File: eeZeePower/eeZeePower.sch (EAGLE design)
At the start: 11 parts

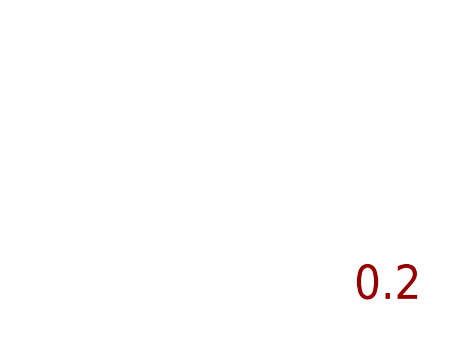
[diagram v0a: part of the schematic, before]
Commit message: Rev 0.3 converted to standard 1206 LED, centered components, mitered corners, moved some components around, removed component names.
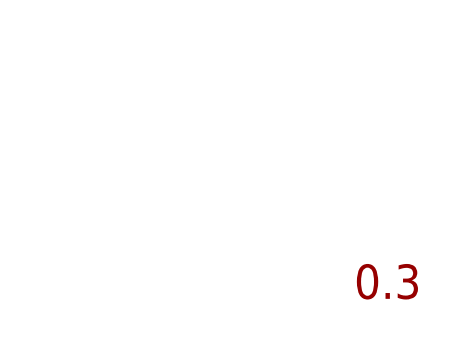
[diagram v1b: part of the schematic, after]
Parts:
- LED1: device led:LEDCHIPLED_0805 -> led:LEDCHIPLED_1206
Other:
- note added: "0.3"
- note removed: "0.2"
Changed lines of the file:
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@@
 <?xml version="1.0" encoding="utf-8"?>
 <!DOCTYPE eagle SYSTEM "eagle.dtd">
-<eagle version="6.3">
+<eagle version="6.4">
 <drawing>
 <settings>
@@
 <grid distance="0.1" unitdist="inch" unit="inch" style="lines" multiple="1" display="no" altdistance="0.01" altunitdist="inch" altunit="inch"/>
 <layers>
-<layer number="1" name="Top" color="4" fill="1" visible="no" active="no"/>
-<layer number="16" name="Bottom" color="1" fill="1" visible="no" active="no"/>
-<layer number="17" name="Pads" color="2" fill="1" visible="no" active="no"/>
-<layer number="18" name="Vias" color="2" fill="1" visible="no" active="no"/>
-<layer number="19" name="Unrouted" color="6" fill="1" visible="no" active="no"/>
-<layer number="20" name="Dimension" color="15" fill="1" visible="no" active="no"/>
-<layer number="21" name="tPlace" color="7" fill="1" visible="no" active="no"/>
-<layer number="22" name="bPlace" color="7" fill="1" visible="no" active="no"/>
-<layer number="23" name="tOrigins" color="15" fill="1" visible="no" active="no"/>
-<layer number="24" name="bOrigins" color="15" fill="1" visible="no" active="no"/>
-<layer number="25" name="tNames" color="7" fill="1" visible="no" active="no"/>
-<layer number="26" name="bNames" color="7" fill="1" visible="no" active="no"/>
-<layer number="27" name="tValues" color="7" fill="1" visible="no" active="no"/>
-<layer number="28" name="bValues" color="7" fill="1" visible="no" active="no"/>
+<layer number="1" name="Top" color="4" fill="1" visible="yes" active="no"/>
+<layer number="16" name="Bottom" color="1" fill="1" visible="yes" active="no"/>
+<layer number="17" name="Pads" color="2" fill="1" visible="yes" active="no"/>
+<layer number="18" name="Vias" color="2" fill="1" visible="yes" active="no"/>
+<layer number="19" name="Unrouted" color="6" fill="1" visible="yes" active="no"/>
+<layer number="20" name="Dimension" color="15" fill="1" visible="yes" active="no"/>
+<layer number="21" name="tPlace" color="7" fill="1" visible="yes" active="no"/>
+<layer number="22" name="bPlace" color="7" fill="1" visible="yes" active="no"/>
+<layer number="23" name="tOrigins" color="15" fill="1" visible="yes" active="no"/>
+<layer number="24" name="bOrigins" color="15" fill="1" visible="yes" active="no"/>
+<layer number="25" name="tNames" color="7" fill="1" visible="yes" active="no"/>
+<layer number="26" name="bNames" color="7" fill="1" visible="yes" active="no"/>
+<layer number="27" name="tValues" color="7" fill="1" visible="yes" active="no"/>
+<layer number="28" name="bValues" color="7" fill="1" visible="yes" active="no"/>
 <layer number="29" name="tStop" color="7" fill="3" visible="no" active="no"/>
 <layer number="30" name="bStop" color="7" fill="6" visible="no" active="no"/>
@@
 <layer number="35" name="tGlue" color="7" fill="4" visible="no" active="no"/>
 <layer number="36" name="bGlue" color="7" fill="5" visible="no" active="no"/>
-<layer number="37" name="tTest" color="7" fill="1" visible="no" active="no"/>
-<layer number="38" name="bTest" color="7" fill="1" visible="no" active="no"/>
+<layer number="37" name="tTest" color="7" fill="1" visible="yes" active="no"/>
+<layer number="38" name="bTest" color="7" fill="1" visible="yes" active="no"/>
 <layer number="39" name="tKeepout" color="4" fill="11" visible="no" active="no"/>
 <layer number="40" name="bKeepout" color="1" fill="11" visible="no" active="no"/>
@@
 <layer number="44" name="Drills" color="7" fill="1" visible="no" active="no"/>
 <layer number="45" name="Holes" color="7" fill="1" visible="no" active="no"/>
-<layer number="46" name="Milling" color="3" fill="1" visible="no" active="no"/>
-<layer number="47" name="Measures" color="7" fill="1" visible="no" active="no"/>
-<layer number="48" name="Document" color="7" fill="1" visible="no" active="no"/>
-<layer number="49" name="Reference" color="7" fill="1" visible="no" active="no"/>
-<layer number="50" name="dxf" color="7" fill="1" visible="no" active="no"/>
-<layer number="51" name="tDocu" color="7" fill="1" visible="no" active="no"/>
-<layer number="52" name="bDocu" color="7" fill="1" visible="no" active="no"/>
-<layer number="53" name="tGND_GNDA" color="7" fill="9" visible="no" active="no"/>
-<layer number="54" name="bGND_GNDA" color="1" fill="9" visible="no" active="no"/>
-<layer number="56" name="wert" color="7" fill="1" visible="no" active="no"/>
+<layer number="46" name="Milling" color="3" fill="1" visible="yes" active="no"/>
+<layer number="47" name="Measures" color="7" fill="1" visible="yes" active="no"/>
+<layer number="48" name="Document" color="7" fill="1" visible="yes" active="no"/>
+<layer number="49" name="Reference" color="7" fill="1" visible="yes" active="no"/>
+<layer number="50" name="dxf" color="7" fill="1" visible="yes" active="no"/>
+<layer number="51" name="tDocu" color="7" fill="1" visible="yes" active="no"/>
+<layer number="52" name="bDocu" color="7" fill="1" visible="yes" active="no"/>
+<layer number="53" name="tGND_GNDA" color="7" fill="9" visible="yes" active="no"/>
+<layer number="54" name="bGND_GNDA" color="1" fill="9" visible="yes" active="no"/>
+<layer number="56" name="wert" color="7" fill="1" visible="yes" active="no"/>
 <layer number="91" name="Nets" color="2" fill="1" visible="yes" active="yes"/>
 <layer number="92" name="Busses" color="1" fill="1" visible="yes" active="yes"/>
@@
 <part name="JP10" library="pinhead-2" deviceset="PINHD-1X03" device="_2.54-S" value="SEL"/>
 <part name="GND2" library="mes" deviceset="GND" device=""/>
-<part name="LED1" library="led" deviceset="LED" device="CHIPLED_0805"/>
+<part name="LED1" library="led" deviceset="LED" device="CHIPLED_1206"/>
 <part name="C1" library="rcl" deviceset="C-US" device="C0603" value="0.1uF"/>
 <part name="C2" library="rcl" deviceset="CPOL-US" device="SMCB" value="100uF"/>
@@
 <plain>
 <text x="160.528" y="23.622" size="3.81" layer="94">eeZee Power</text>
-<text x="233.934" y="24.13" size="3.81" layer="94">0.2</text>
+<text x="233.934" y="24.13" size="3.81" layer="94">0.3</text>
 <text x="55.88" y="134.62" size="1.778" layer="91">NOTE: determine cause of short when rail powered and eeZee Power inserted reverse polarity</text>
 </plain>

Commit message: Converted to standard 1206 10uF, placed input bypass caps on bottom. Rearranged silk, centered pin headers.
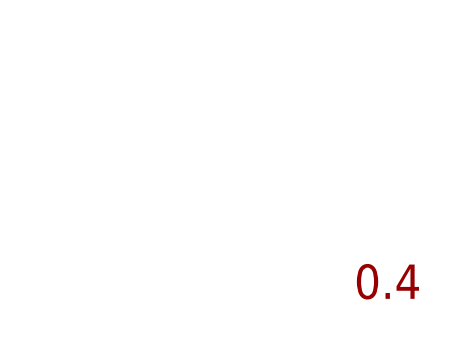
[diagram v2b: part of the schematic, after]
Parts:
- C3: device rcl:C-USC0603 -> rcl:C-USC1206
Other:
- note added: "0.4"
- note removed: "0.3"
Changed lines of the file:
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@@
 <part name="C2" library="rcl" deviceset="CPOL-US" device="SMCB" value="100uF"/>
 <part name="R1" library="resistor" deviceset="R-US_" device="R0603"/>
-<part name="C3" library="rcl" deviceset="C-US" device="C0603" value="10uF"/>
+<part name="C3" library="rcl" deviceset="C-US" device="C1206" value="10uF"/>
 <part name="FRAME1" library="mes" deviceset="LETTER_L" device=""/>
 <part name="C4" library="rcl" deviceset="C-US" device="C0603" value="0.1uF"/>
@@
 <plain>
 <text x="160.528" y="23.622" size="3.81" layer="94">eeZee Power</text>
-<text x="233.934" y="24.13" size="3.81" layer="94">0.3</text>
+<text x="233.934" y="24.13" size="3.81" layer="94">0.4</text>
 <text x="55.88" y="134.62" size="1.778" layer="91">NOTE: determine cause of short when rail powered and eeZee Power inserted reverse polarity</text>
 </plain>

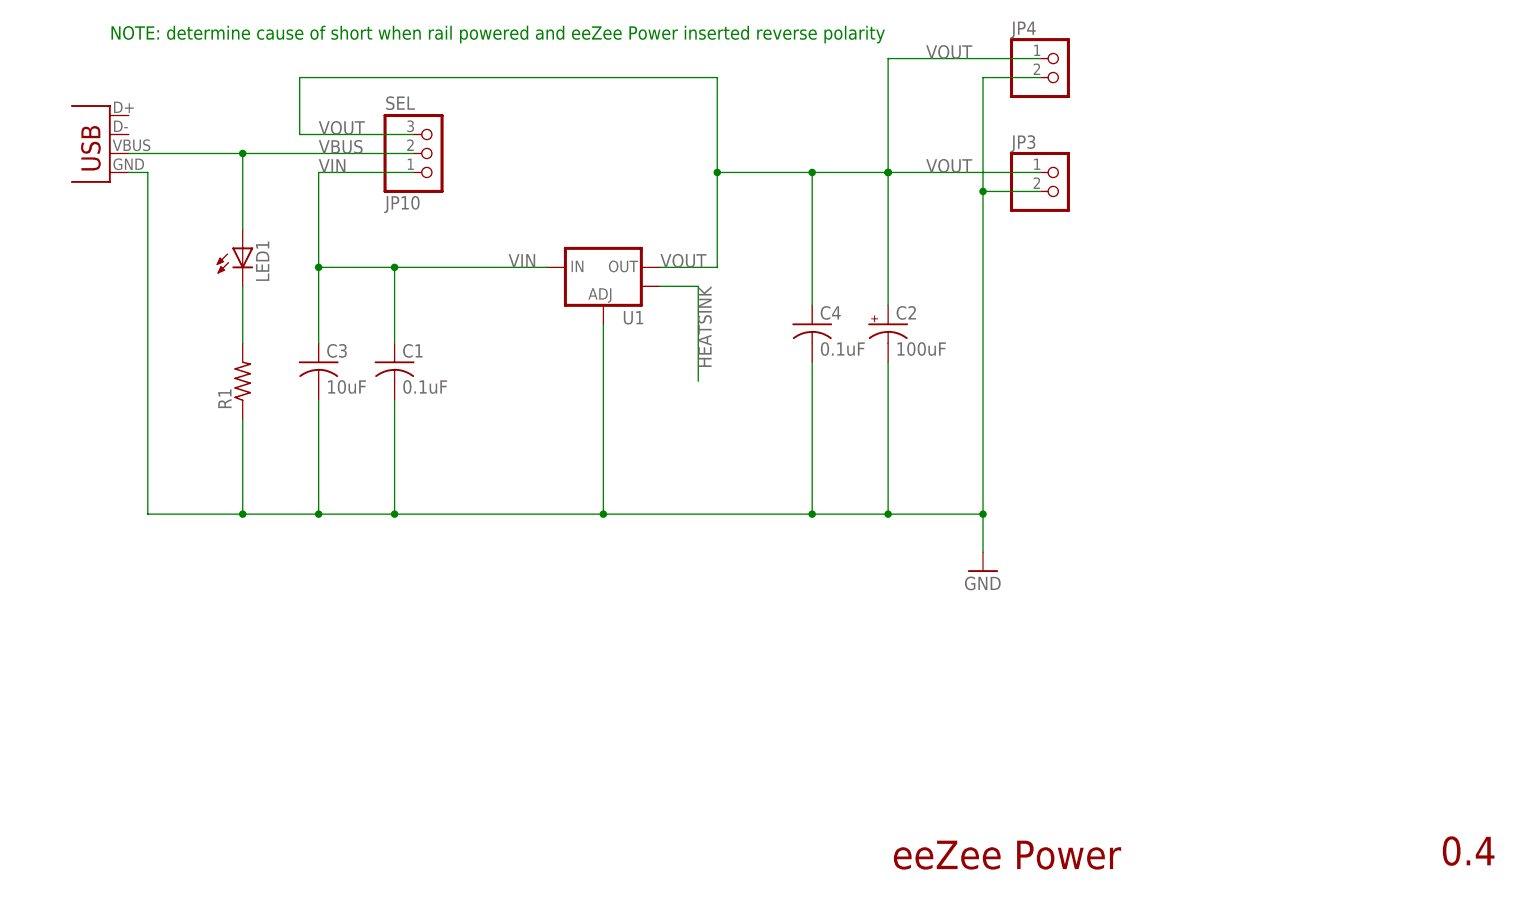
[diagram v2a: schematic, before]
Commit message: Changed to 10mil/8mil spacing, improved thermal design, connected heatsink to VOUT.
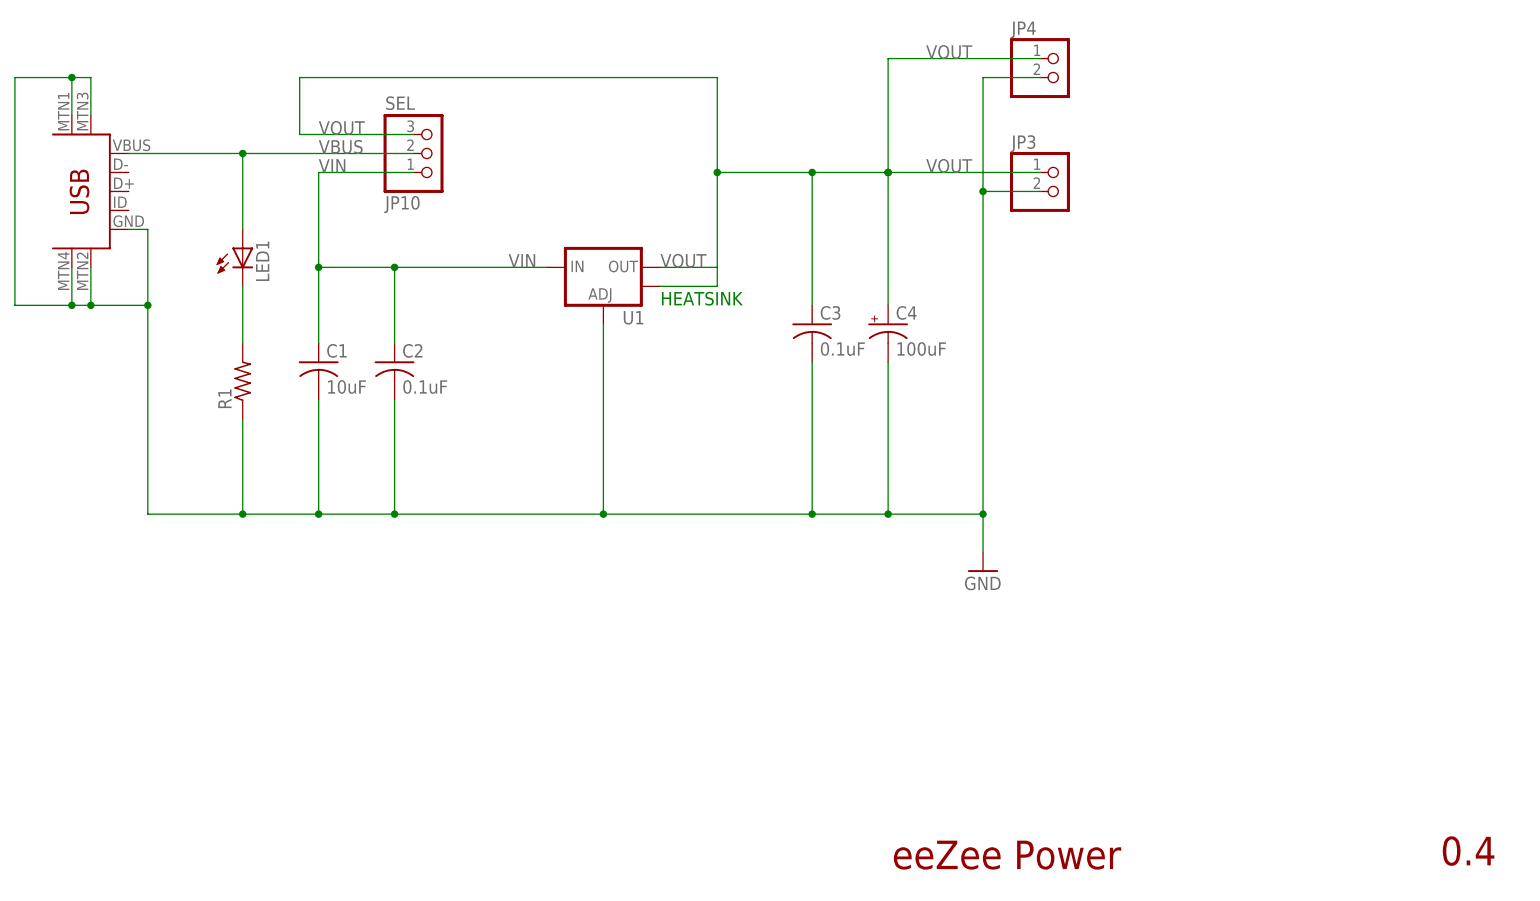
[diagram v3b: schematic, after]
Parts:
- removed JP1: USBSMD, SparkFun:USBSMD
- added U$1: USB-MINIB-5PIN, SparkFun:USB-MINIB-5PIN
- C1: value 0.1uF -> 10uF; device rcl:C-USC0603 -> rcl:C-USC1206
- C2: value 100uF -> 0.1uF; device rcl:CPOL-USSMCB -> rcl:C-USC0603
- C3: value 10uF -> 0.1uF; device rcl:C-USC1206 -> rcl:C-USC0603
- C4: value 0.1uF -> 100uF; device rcl:C-USC0603 -> rcl:CPOL-USSMCB
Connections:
- removed net HEATSINK: U1.OUT@1
- net GND: now also C2.2, C4.-, U$1.GND, U$1.MTN1, U$1.MTN2, U$1.MTN3, U$1.MTN4; no longer C2.-, C4.2, JP1.GND
- net VBUS: now also U$1.VBUS; no longer JP1.VBUS
- net VIN: now also C2.1; no longer C3.1
- net VOUT: now also C3.1, C4.+, U1.OUT@1; no longer C2.+, C4.1
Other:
- note added: "HEATSINK"
- note removed: "NOTE: determine cause of short when rail powered and eeZee Power inserted reverse polarity"
- moved on the sheet: C1, C3

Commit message: Updated version #
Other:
- note added: "0.5"
- note removed: "0.4"
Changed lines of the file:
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@@
 <plain>
 <text x="160.528" y="23.622" size="3.81" layer="94">eeZee Power</text>
-<text x="233.934" y="24.13" size="3.81" layer="94">0.4</text>
+<text x="233.934" y="24.13" size="3.81" layer="94">0.5</text>
 <text x="129.54" y="99.06" size="1.778" layer="91">HEATSINK</text>
 </plain>
